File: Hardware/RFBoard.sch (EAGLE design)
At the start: 388 parts, among them IC1 HMC1097, IC10 NCP702-1.8, IC11 TPS42951, IC12 MCP4812, IC13 STM32F030C8T, IC14 LT5560, IC15 ADF4360, IC16 HMC284, IC17 HMC284, IC18 NCP702-3.3, IC19 NCP702-3.3, IC2 MAX2871, IC20 LT1395, IC21 MAADSS0008, IC22 MAADSS0008, IC23 MAADSS0008, IC24 RFSA2033, IC25 MMG3H21NT1, IC26 MMG3H21NT1, IC27 HMC1021, IC28 MCP4812, IC29 NCP702-3.3, IC3 AP2114HA-3.3, IC31 QPC6064, IC32 QPC6064, IC4 NCP702-3.3, IC5 NCP702-3.3, IC6 MAX5873, IC7 NCP702-1.8, IC8 NCP702-3.3, IC9 NCP702-3.3, Q1 BSS123, Q2 BSS123, Q3 BSS123, Q4 BSS123, Q5 BSS123, Q6 BSS84, U1 6SLX9TQG144, U4 W25Q16BVSN, X1 out, X2 FH12-20S-0.5SH

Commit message: PCB finished
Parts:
- added C184: 100n, rcl:C-EUC0603
- added J1: U.FL-R-SMT, connector:U.FL-R-SMT
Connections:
- new net N$178: C184.2, J1.ANT
- net 10MHZ_REF: now also C184.1
- net GND: now also J1.P$2
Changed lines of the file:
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@@
 <layer number="54" name="bPadExt" color="1" fill="1" visible="no" active="no"/>
 <layer number="56" name="wert" color="7" fill="1" visible="no" active="no"/>
+<layer number="57" name="tCAD" color="7" fill="1" visible="no" active="no"/>
 <layer number="88" name="SimResults" color="9" fill="1" visible="yes" active="yes"/>
 <layer number="89" name="SimProbes" color="9" fill="1" visible="yes" active="yes"/>
@@
 <layer number="99" name="SpiceOrder" color="5" fill="1" visible="yes" active="yes"/>
 <layer number="100" name="Muster" color="7" fill="1" visible="no" active="no"/>
+<layer number="101" name="Patch_Top" color="12" fill="4" visible="yes" active="yes"/>
+<layer number="102" name="Vscore" color="7" fill="1" visible="yes" active="yes"/>
+<layer number="103" name="tMap" color="7" fill="1" visible="yes" active="yes"/>
+<layer number="104" name="Name" color="16" fill="1" visible="yes" active="yes"/>
+<layer number="105" name="tPlate" color="7" fill="1" visible="yes" active="yes"/>
+<layer number="106" name="bPlate" color="7" fill="1" visible="yes" active="yes"/>
+<layer number="107" name="Crop" color="2" fill="1" visible="yes" active="yes"/>
+<layer number="108" name="fp8" color="7" fill="1" visible="yes" active="yes"/>
+<layer number="109" name="fp9" color="7" fill="1" visible="yes" active="yes"/>
+<layer number="110" name="fp0" color="7" fill="1" visible="yes" active="yes"/>
+<layer number="111" name="LPC17xx" color="7" fill="1" visible="yes" active="yes"/>
+<layer number="112" name="tSilk" color="7" fill="1" visible="yes" active="yes"/>
+<layer number="113" name="IDFDebug" color="7" fill="1" visible="yes" active="yes"/>
+<layer number="116" name="Patch_BOT" color="9" fill="4" visible="yes" active="yes"/>
+<layer number="121" name="_tsilk" color="7" fill="1" visible="yes" active="yes"/>
+<layer number="122" name="_bsilk" color="7" fill="1" visible="yes" active="yes"/>
+<layer number="123" name="tTestmark" color="7" fill="1" visible="yes" active="yes"/>
+<layer number="124" name="bTestmark" color="7" fill="1" visible="yes" active="yes"/>
+<layer number="125" name="_tNames" color="7" fill="1" visible="yes" active="yes"/>
+<layer number="126" name="_bNames" color="7" fill="1" visible="yes" active="yes"/>
+<layer number="127" name="_tValues" color="7" fill="1" visible="yes" active="yes"/>
+<layer number="128" name="_bValues" color="7" fill="1" visible="yes" active="yes"/>
+<layer number="131" name="tAdjust" color="7" fill="1" visible="yes" active="yes"/>
+<layer number="132" name="bAdjust" color="7" fill="1" visible="yes" active="yes"/>
+<layer number="144" name="Drill_legend" color="7" fill="1" visible="yes" active="yes"/>
+<layer number="150" name="Notes" color="7" fill="1" visible="yes" active="yes"/>
+<layer number="151" name="HeatSink" color="7" fill="1" visible="yes" active="yes"/>
+<layer number="152" name="_bDocu" color="7" fill="1" visible="yes" active="yes"/>
+<layer number="153" name="FabDoc1" color="7" fill="1" visible="yes" active="yes"/>
+<layer number="154" name="FabDoc2" color="7" fill="1" visible="yes" active="yes"/>
+<layer number="155" name="FabDoc3" color="7" fill="1" visible="yes" active="yes"/>
+<layer number="199" name="Contour" color="7" fill="1" visible="yes" active="yes"/>
+<layer number="200" name="200bmp" color="1" fill="10" visible="yes" active="yes"/>
+<layer number="201" name="201bmp" color="1" fill="10" visible="yes" active="yes"/>
+<layer number="202" name="202bmp" color="3" fill="10" visible="yes" active="yes"/>
+<layer number="203" name="203bmp" color="4" fill="10" visible="yes" active="yes"/>
+<layer number="204" name="204bmp" color="5" fill="10" visible="yes" active="yes"/>
+<layer number="205" name="205bmp" color="6" fill="10" visible="yes" active="yes"/>
+<layer number="206" name="206bmp" color="7" fill="10" visible="yes" active="yes"/>
+<layer number="207" name="207bmp" color="8" fill="10" visible="yes" active="yes"/>
+<layer number="208" name="208bmp" color="9" fill="10" visible="yes" active="yes"/>
+<layer number="209" name="209bmp" color="7" fill="1" visible="yes" active="yes"/>
+<layer number="210" name="210bmp" color="7" fill="1" visible="yes" active="yes"/>
+<layer number="211" name="211bmp" color="7" fill="1" visible="yes" active="yes"/>
+<layer number="212" name="212bmp" color="7" fill="1" visible="yes" active="yes"/>
+<layer number="213" name="213bmp" color="7" fill="1" visible="yes" active="yes"/>
+<layer number="214" name="214bmp" color="7" fill="1" visible="yes" active="yes"/>
+<layer number="215" name="215bmp" color="7" fill="1" visible="yes" active="yes"/>
+<layer number="216" name="216bmp" color="7" fill="1" visible="yes" active="yes"/>
+<layer number="217" name="217bmp" color="18" fill="1" visible="no" active="no"/>
+<layer number="218" name="218bmp" color="19" fill="1" visible="no" active="no"/>
+<layer number="219" name="219bmp" color="20" fill="1" visible="no" active="no"/>
+<layer number="220" name="220bmp" color="21" fill="1" visible="no" active="no"/>
+<layer number="221" name="221bmp" color="22" fill="1" visible="no" active="no"/>
+<layer number="222" name="222bmp" color="23" fill="1" visible="no" active="no"/>
+<layer number="223" name="223bmp" color="24" fill="1" visible="no" active="no"/>
+<layer number="224" name="224bmp" color="25" fill="1" visible="no" active="no"/>
+<layer number="248" name="Housing" color="7" fill="1" visible="yes" active="yes"/>
+<layer number="249" name="Edge" color="7" fill="1" visible="yes" active="yes"/>
 <layer number="250" name="Descript" color="3" fill="1" visible="no" active="no"/>
 <layer number="251" name="SMDround" color="12" fill="11" visible="no" active="no"/>
+<layer number="254" name="cooling" color="7" fill="1" visible="yes" active="yes"/>
 </layers>
 <schematic xreflabel="%F%N/%S.%C%R" xrefpart="/%S.%C%R">
@@
 <part name="GND210" library="supply1" deviceset="GND" device=""/>
 <part name="GND211" library="supply1" deviceset="GND" device=""/>
+<part name="J1" library="connector" deviceset="U.FL-R-SMT" device=""/>
+<part name="GND212" library="supply1" deviceset="GND" device=""/>
+<part name="C184" library="rcl" deviceset="C-EU" device="C0603" value="100n"/>
 </parts>
 <sheets>
@@
 <attribute name="VALUE" x="91.44" y="48.26" size="1.778" layer="96"/>
 </instance>
+<instance part="J1" gate="G$1" x="127" y="170.18" smashed="yes">
+<attribute name="NAME" x="127" y="173.228" size="1.27" layer="95"/>
+<attribute name="VALUE" x="129.54" y="167.64" size="1.27" layer="96"/>
+</instance>
+<instance part="GND212" gate="1" x="127" y="162.56" smashed="yes" rot="MR0">
+<attribute name="VALUE" x="129.54" y="160.02" size="1.778" layer="96" rot="MR0"/>
+</instance>
+<instance part="C184" gate="G$1" x="116.84" y="170.18" smashed="yes" rot="R90">
+<attribute name="NAME" x="116.459" y="171.704" size="1.778" layer="95" rot="R90"/>
+<attribute name="VALUE" x="121.539" y="171.704" size="1.778" layer="96" rot="R90"/>
+</instance>
 </instances>
 <busses>
@@
 <wire x1="93.98" y1="53.34" x2="93.98" y2="55.88" width="0.1524" layer="91"/>
 </segment>
+<segment>
+<pinref part="J1" gate="G$1" pin="P$2"/>
+<pinref part="GND212" gate="1" pin="GND"/>
+</segment>
 </net>
 <net name="I0" class="0">
@@
 <pinref part="R76" gate="G$1" pin="1"/>
 <wire x1="104.14" y1="127" x2="111.76" y2="127" width="0.1524" layer="91"/>
-<label x="111.76" y="129.54" size="1.778" layer="95" rot="R90" xref="yes"/>
-<wire x1="111.76" y1="127" x2="111.76" y2="129.54" width="0.1524" layer="91"/>
+<label x="109.22" y="170.18" size="1.778" layer="95" rot="R180" xref="yes"/>
+<wire x1="111.76" y1="127" x2="111.76" y2="170.18" width="0.1524" layer="91"/>
+<wire x1="111.76" y1="170.18" x2="109.22" y2="170.18" width="0.1524" layer="91"/>
+<pinref part="C184" gate="G$1" pin="1"/>
+<wire x1="114.3" y1="170.18" x2="111.76" y2="170.18" width="0.1524" layer="91"/>
+<junction x="111.76" y="170.18"/>
 </segment>
 </net>
@@
 </segment>
 </net>
+<net name="N$178" class="0">
+<segment>
+<pinref part="C184" gate="G$1" pin="2"/>
+<pinref part="J1" gate="G$1" pin="ANT"/>
+<wire x1="121.92" y1="170.18" x2="124.46" y2="170.18" width="0.1524" layer="91"/>
+</segment>
+</net>
 </nets>
 </sheet>
@@
 </sheet>
 </sheets>
+<errors>
+</errors>
 </schematic>
 </drawing>

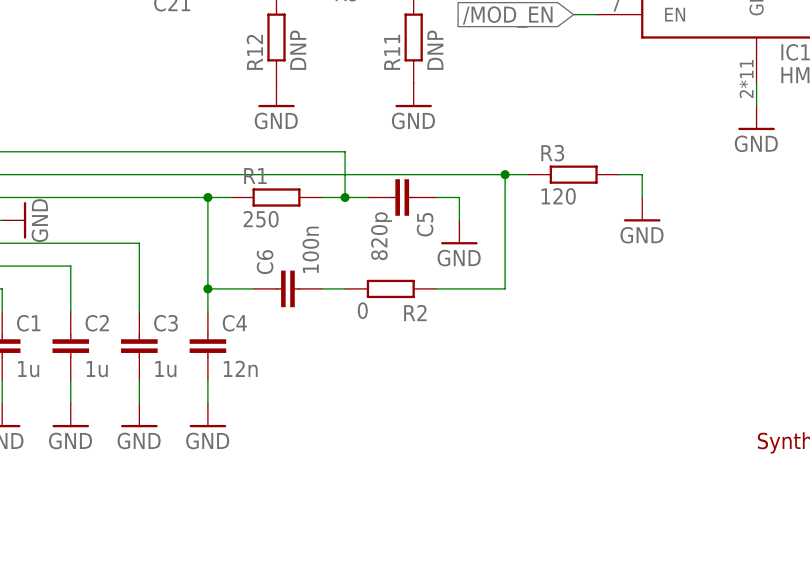
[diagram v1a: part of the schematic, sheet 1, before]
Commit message: PLL loop filter values changed
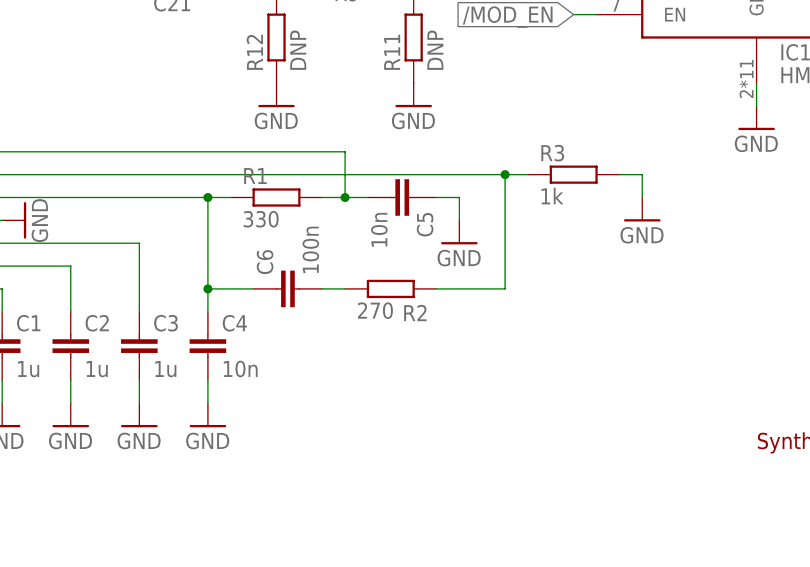
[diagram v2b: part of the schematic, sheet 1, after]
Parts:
- C102, C5: value 820p -> 10n
- C103: value 100n -> 330p
- C104: value 820p -> 220p
- C4: value 12n -> 10n
- R1: value 250 -> 330
- R15: value 73k2 -> 15k
- R2: value 0 -> 270
- R27: value 250 -> 15k
- R29: value 120 -> 6k8
- R3: value 120 -> 1k
- R66: value 22k1 -> 11k
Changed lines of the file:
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@@
 <part name="GND1" library="supply1" deviceset="GND" device=""/>
 <part name="GND2" library="supply1" deviceset="GND" device=""/>
-<part name="R1" library="resistor" deviceset="R-EU_" device="R0603" value="250"/>
-<part name="R2" library="resistor" deviceset="R-EU_" device="R0603" value="0"/>
-<part name="R3" library="resistor" deviceset="R-EU_" device="R0603" value="120"/>
+<part name="R1" library="resistor" deviceset="R-EU_" device="R0603" value="330"/>
+<part name="R2" library="resistor" deviceset="R-EU_" device="R0603" value="270"/>
+<part name="R3" library="resistor" deviceset="R-EU_" device="R0603" value="1k"/>
 <part name="C1" library="rcl" deviceset="C-EU" device="C0603" value="1u"/>
 <part name="C2" library="rcl" deviceset="C-EU" device="C0603" value="1u"/>
 <part name="C3" library="rcl" deviceset="C-EU" device="C0603" value="1u"/>
-<part name="C4" library="rcl" deviceset="C-EU" device="C0603" value="12n"/>
-<part name="C5" library="rcl" deviceset="C-EU" device="C0603" value="820p"/>
+<part name="C4" library="rcl" deviceset="C-EU" device="C0603" value="10n"/>
+<part name="C5" library="rcl" deviceset="C-EU" device="C0603" value="10n"/>
 <part name="C6" library="rcl" deviceset="C-EU" device="C0603" value="100n"/>
 <part name="GND3" library="supply1" deviceset="GND" device=""/>
@@
 <part name="IC16" library="rf" deviceset="HMC284" device=""/>
 <part name="IC17" library="rf" deviceset="HMC284" device=""/>
-<part name="R27" library="resistor" deviceset="R-EU_" device="R0603" value="250"/>
-<part name="R29" library="resistor" deviceset="R-EU_" device="R0603" value="120"/>
+<part name="R27" library="resistor" deviceset="R-EU_" device="R0603" value="15k"/>
+<part name="R29" library="resistor" deviceset="R-EU_" device="R0603" value="6k8"/>
 <part name="C101" library="rcl" deviceset="C-EU" device="C0603" value="10n"/>
-<part name="C102" library="rcl" deviceset="C-EU" device="C0603" value="820p"/>
-<part name="C103" library="rcl" deviceset="C-EU" device="C0603" value="100n"/>
+<part name="C102" library="rcl" deviceset="C-EU" device="C0603" value="10n"/>
+<part name="C103" library="rcl" deviceset="C-EU" device="C0603" value="330p"/>
 <part name="R30" library="resistor" deviceset="R-EU_" device="R0603" value="4k7"/>
-<part name="C104" library="rcl" deviceset="C-EU" device="C0603" value="820p"/>
+<part name="C104" library="rcl" deviceset="C-EU" device="C0603" value="220p"/>
 <part name="C105" library="rcl" deviceset="C-EU" device="C0603" value="10u"/>
 <part name="L50" library="rf" deviceset="INDUCTOR" device="0603" value="100n"/>
@@
 <part name="C164" library="rcl" deviceset="C-EU" device="C1206" value="22u"/>
 <part name="C165" library="rcl" deviceset="C-EU" device="C1206" value="22u"/>
-<part name="R15" library="resistor" deviceset="R-EU_" device="R0603" value="73k2"/>
-<part name="R66" library="resistor" deviceset="R-EU_" device="R0603" value="22k1"/>
+<part name="R15" library="resistor" deviceset="R-EU_" device="R0603" value="15k"/>
+<part name="R66" library="resistor" deviceset="R-EU_" device="R0603" value="11k"/>
 <part name="GND179" library="supply1" deviceset="GND" device=""/>
 <part name="GND180" library="supply1" deviceset="GND" device=""/>

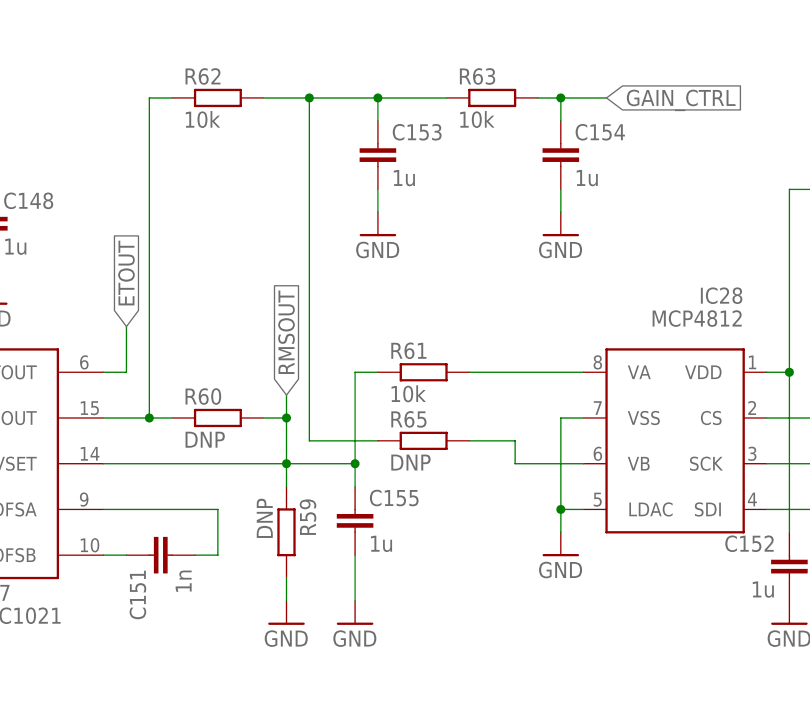
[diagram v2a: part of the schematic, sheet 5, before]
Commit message: Value changes amplitude control feedback loop
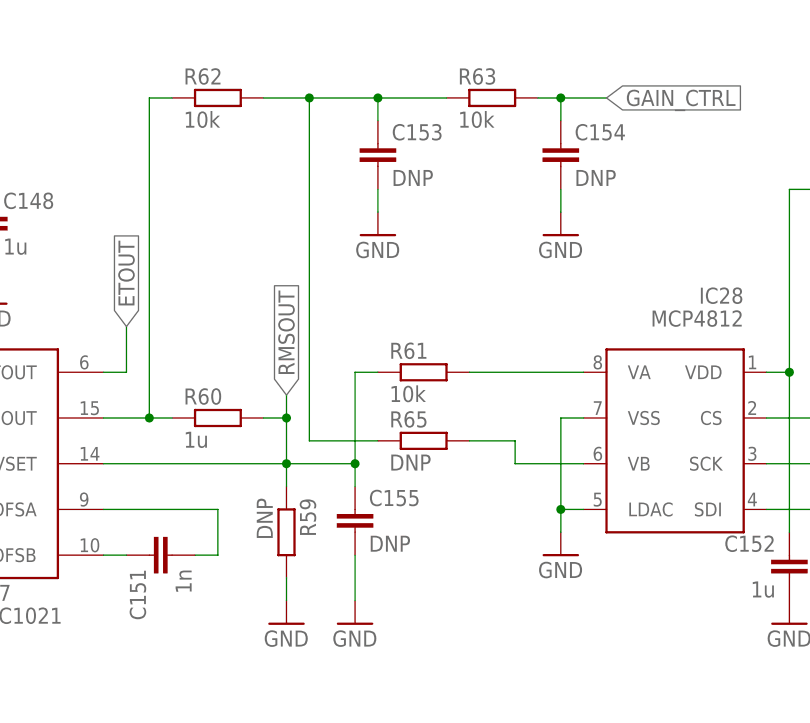
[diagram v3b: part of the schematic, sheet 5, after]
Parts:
- C153, C154, C155: value 1u -> DNP
- R60: value DNP -> 1u
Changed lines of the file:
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@@
 <part name="GND160" library="supply1" deviceset="GND" device=""/>
 <part name="R59" library="resistor" deviceset="R-EU_" device="R0603" value="DNP"/>
-<part name="R60" library="resistor" deviceset="R-EU_" device="R0603" value="DNP"/>
+<part name="R60" library="resistor" deviceset="R-EU_" device="R0603" value="1u"/>
 <part name="GND161" library="supply1" deviceset="GND" device=""/>
 <part name="R61" library="resistor" deviceset="R-EU_" device="R0603" value="10k"/>
 <part name="R62" library="resistor" deviceset="R-EU_" device="R0603" value="10k"/>
-<part name="C153" library="rcl" deviceset="C-EU" device="C0603" value="1u"/>
+<part name="C153" library="rcl" deviceset="C-EU" device="C0603" value="DNP"/>
 <part name="R63" library="resistor" deviceset="R-EU_" device="R0603" value="10k"/>
-<part name="C154" library="rcl" deviceset="C-EU" device="C0603" value="1u"/>
+<part name="C154" library="rcl" deviceset="C-EU" device="C0603" value="DNP"/>
 <part name="GND162" library="supply1" deviceset="GND" device=""/>
 <part name="GND163" library="supply1" deviceset="GND" device=""/>
-<part name="C155" library="rcl" deviceset="C-EU" device="C0603" value="1u"/>
+<part name="C155" library="rcl" deviceset="C-EU" device="C0603" value="DNP"/>
 <part name="GND164" library="supply1" deviceset="GND" device=""/>
 <part name="R64" library="resistor" deviceset="R-EU_" device="R0603" value="10k"/>

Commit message: External modulation input usable as modulation source
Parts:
- C4: value 10n -> 2n
- C5: value 10n -> 180p
- C6: value 100n -> 33n
- R1: value 330 -> 1k
- R2: value 270 -> 100
- R3: value 1k -> 120
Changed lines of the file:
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@@
 <part name="GND1" library="supply1" deviceset="GND" device=""/>
 <part name="GND2" library="supply1" deviceset="GND" device=""/>
-<part name="R1" library="resistor" deviceset="R-EU_" device="R0603" value="330"/>
-<part name="R2" library="resistor" deviceset="R-EU_" device="R0603" value="270"/>
-<part name="R3" library="resistor" deviceset="R-EU_" device="R0603" value="1k"/>
+<part name="R1" library="resistor" deviceset="R-EU_" device="R0603" value="1k"/>
+<part name="R2" library="resistor" deviceset="R-EU_" device="R0603" value="100"/>
+<part name="R3" library="resistor" deviceset="R-EU_" device="R0603" value="120"/>
 <part name="C1" library="rcl" deviceset="C-EU" device="C0603" value="1u"/>
 <part name="C2" library="rcl" deviceset="C-EU" device="C0603" value="1u"/>
 <part name="C3" library="rcl" deviceset="C-EU" device="C0603" value="1u"/>
-<part name="C4" library="rcl" deviceset="C-EU" device="C0603" value="10n"/>
-<part name="C5" library="rcl" deviceset="C-EU" device="C0603" value="10n"/>
-<part name="C6" library="rcl" deviceset="C-EU" device="C0603" value="100n"/>
+<part name="C4" library="rcl" deviceset="C-EU" device="C0603" value="2n"/>
+<part name="C5" library="rcl" deviceset="C-EU" device="C0603" value="180p"/>
+<part name="C6" library="rcl" deviceset="C-EU" device="C0603" value="33n"/>
 <part name="GND3" library="supply1" deviceset="GND" device=""/>
 <part name="GND4" library="supply1" deviceset="GND" device=""/>
